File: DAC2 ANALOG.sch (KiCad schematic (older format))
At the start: 66 parts

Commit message: Add files via upload
Final - added testpoints, added MANF# data. Removed reconstruction filter
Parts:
- removed C? (x4): 6800pF, SciMod:EIA0603, symbol SciLib:C
- removed C? (x11): .1uF, SciMod:EIA0603, symbol Device:C
- removed C? (x2): 10uF, SciMod:EIA3528, symbol SciLib:CP1
- removed C?: 10pF, SciMod:EIA0603, symbol Device:C
- removed J?: SMB, SciMod:SMB 50, symbol SciLib:BNC
- removed J?: DAC BUFF, SciMod:SMB 50, symbol SciLib:BNC
- removed R? (x4): 10K, SciMod:EIA0603, symbol Device:R
- removed R? (x2): 33, SciMod:EIA0402, symbol SciLib:R
- removed TP?: VrefP, SciMod:TESTPOINT, symbol Connector:TestPoint
- removed TP?: VrefN, SciMod:TESTPOINT, symbol Connector:TestPoint
- removed TP?: AGND, SciMod:TESTPOINT, symbol Connector:TestPoint
- removed U?: OPA277, SOIC127P600X175-8N, symbol SciLib:OPA277
- added AGND, DAC: TST, TESTPOINT, symbol SciLib:TST
- added C? (x11): .1uF, SciMod:EIA0603, symbol Device:C
- added C? (x2): 10uF, SciMod:EIA3528, symbol SciLib:CP1
- added C? (x2): 6800pF, SciMod:EIA0805, symbol SciLib:C
- added R?: 0, SciMod:EIA0603, symbol SciLib:R
- added R? (x4): 10K, SciMod:EIA0603, symbol Device:R
- added R? (x2): 33, SciMod:EIA0402, symbol SciLib:R
- added TP?: AD IN, TESTPOINT, symbol SciLib:TST
- added TP?: VRP, TESTPOINT, symbol SciLib:TST
- added TP?: VRN, SciMod:TESTPOINT, symbol SciLib:TST
- C?: footprint SciMod:EIA0603 -> SciMod:EIA0805; Description CAP .1MF 10V 10% X7R EIA0603 -> 6800pF ±2% 50V Ceramic Capacitor C0G, NP0 0805; MANF# (none) -> GRM2195C1H682GA01D; Mfg AVX -> (none); Mfg Pn 0603YC104KAT2A -> (none); Partnum 10954 -> (none)
- C?: Description CAP .1MF 10V 10% X7R EIA0603 -> 47µF ±20% 6.3V Ceramic Capacitor X7R 1210; MANF# (none) -> C1210C476M9RACTU; Mfg AVX -> (none); Mfg Pn 0603YC104KAT2A -> (none); Partnum 10954 -> (none)
- C?: MANF# (none) -> 0603YC104KAT2A; Mfg Pn 0603YC104KAT2A -> (none)
- C?: MANF# (none) -> GRM188R71A105KA61D
- C?: Field4 (none) -> GRM188R71A105KA61D
- C? (x4): Description ?????? -> AVX Tant; MANF# (none) -> TAJB106K016RNJ; Partnum XXXXX -> (none)
- C?: Description ?????? -> AVX Tant; Partnum XXXXX -> TAJB106K016RNJ
- C?: Field5 (none) -> CAP CER 0.1UF 25V X8R 0603; MANF# (none) -> C1608X8R1E104K080AA
- H1, H2: renamed from H?; Description ?????? -> (none); Partnum XXXXX -> (none)
- J?: Description ?????? -> (none); MANF# (none) -> Scientech part; Partnum XXXXX -> (none)
- R? (x2): Description ?????? -> RES SMD 30.1 OHM 0.1% 1/6W 0603; MANF# (none) -> RP73PF1J30R1BTDF; Partnum XXXXX -> (none)
- R?: Field5 (none) -> RES SMD 10K OHM 1% 1/10W 0603; MANF# (none) -> ERJ-3EKF1002V
- R?: Field5 (none) -> RES SMD 5K OHM 0.1% 0.15W 0603 25ppm; MANF# (none) -> PNM0603E5001BST5
- R?: Description ?????? -> (none); MANF# (none) -> RC0402FR-0733RL; Partnum XXXXX -> (none)
- R? (x2): Description ?????? -> (none); Partnum XXXXX -> (none)
- R?: Field5 (none) -> RES 10K OHM 0.1% 1/8W 0805 25ppm; MANF# (none) -> ERA-6AEB103V
- Rs?: MANF# (none) -> Scientech
- U?: Field7 AD5791ARUZ-ND -> (none); MANF# (none) -> AD5791ARUZ-ND
- U?: footprint SciMod:SOIC127P-8 -> SciMod:ADA4077-2BRZ-R7; Description IC OPA2350 DUAL OP AMP HISPEED RRIO 8P SOIC -> IC OPAMP GP 2 CIRCUIT 8SOIC; MANF# (none) -> ADA4077-2BRZ-R7; Mfg TEXAS INSTRUMENTS -> Analog Devices; Mfg Pn OPA2350UA -> ADA4077-2BRZ-R7; Partnum XXXXX -> (none)
- U?: footprint SciMod:ADA4077-1BRZ -> SciMod:ADA4077-2BRZ-R7; Description IC OPA2350 DUAL OP AMP HISPEED RRIO 8P SOIC -> IC OPAMP GP 2 CIRCUIT 8SOIC; MANF# (none) -> ADA4077-2BRZ-R7; Mfg TEXAS INSTRUMENTS -> Analog Devices; Mfg Pn OPA2350UA -> (none); Partnum XXXXX -> (none)
- U?: MANF# (none) -> OPA277U; Mfg Pn OPA277U -> (none); Partnum 10986 -> (none)
- U?: MANF# (none) -> LT1010CT; Mfg Pn LT1010CT -> (none)
- U?: MANF# (none) -> LTC6655BHMS8-5#PBF
- U?: footprint SciMod:SOIC127P-8 -> SciMod:ADA4077-2BRZ-R7
- U?: footprint SciMod:ADA4077-1BRZ -> SciMod:ADA4077-2BRZ-R7; Description IC OPA2350 DUAL OP AMP HISPEED RRIO 8P SOIC -> (none); Mfg TEXAS INSTRUMENTS -> (none); Mfg Pn OPA2350UA -> (none); Partnum XXXXX -> (none)
- U?: MANF# (none) -> LTC6363IMS8#TRPBF
- U?: Description IC OPA277 OPAMP DUAL 8P SOIC -> (none); MANF# (none) -> AD8675ARZ; Mfg TEXAS INSTR -> (none); Mfg Pn OPA277U -> (none); Partnum 10986 -> (none)
- U?: footprint (none) -> SciMod:LTC2500CDKD-32-TRPBF; MANF# (none) -> LTC2500CDKD-32#PBF
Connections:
- wire segments 326 -> 324
- no-connect marks 14 -> 12
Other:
- note added: "+5VDC"
- note added: "-5VDC"
- note added: "References from LT6655 ckt below"
- note added: "Select the A/D input by installing only one of these."
- note added: "This is a bipolar +/- 5VDC signal."
- note added: "This is from the LTC2500-32 data sheet page 17."
- note added: "This reference block is right out of the AD5791EVAL circuit."
- note added: "This whole chunk is from the AD5791 evaluation module."

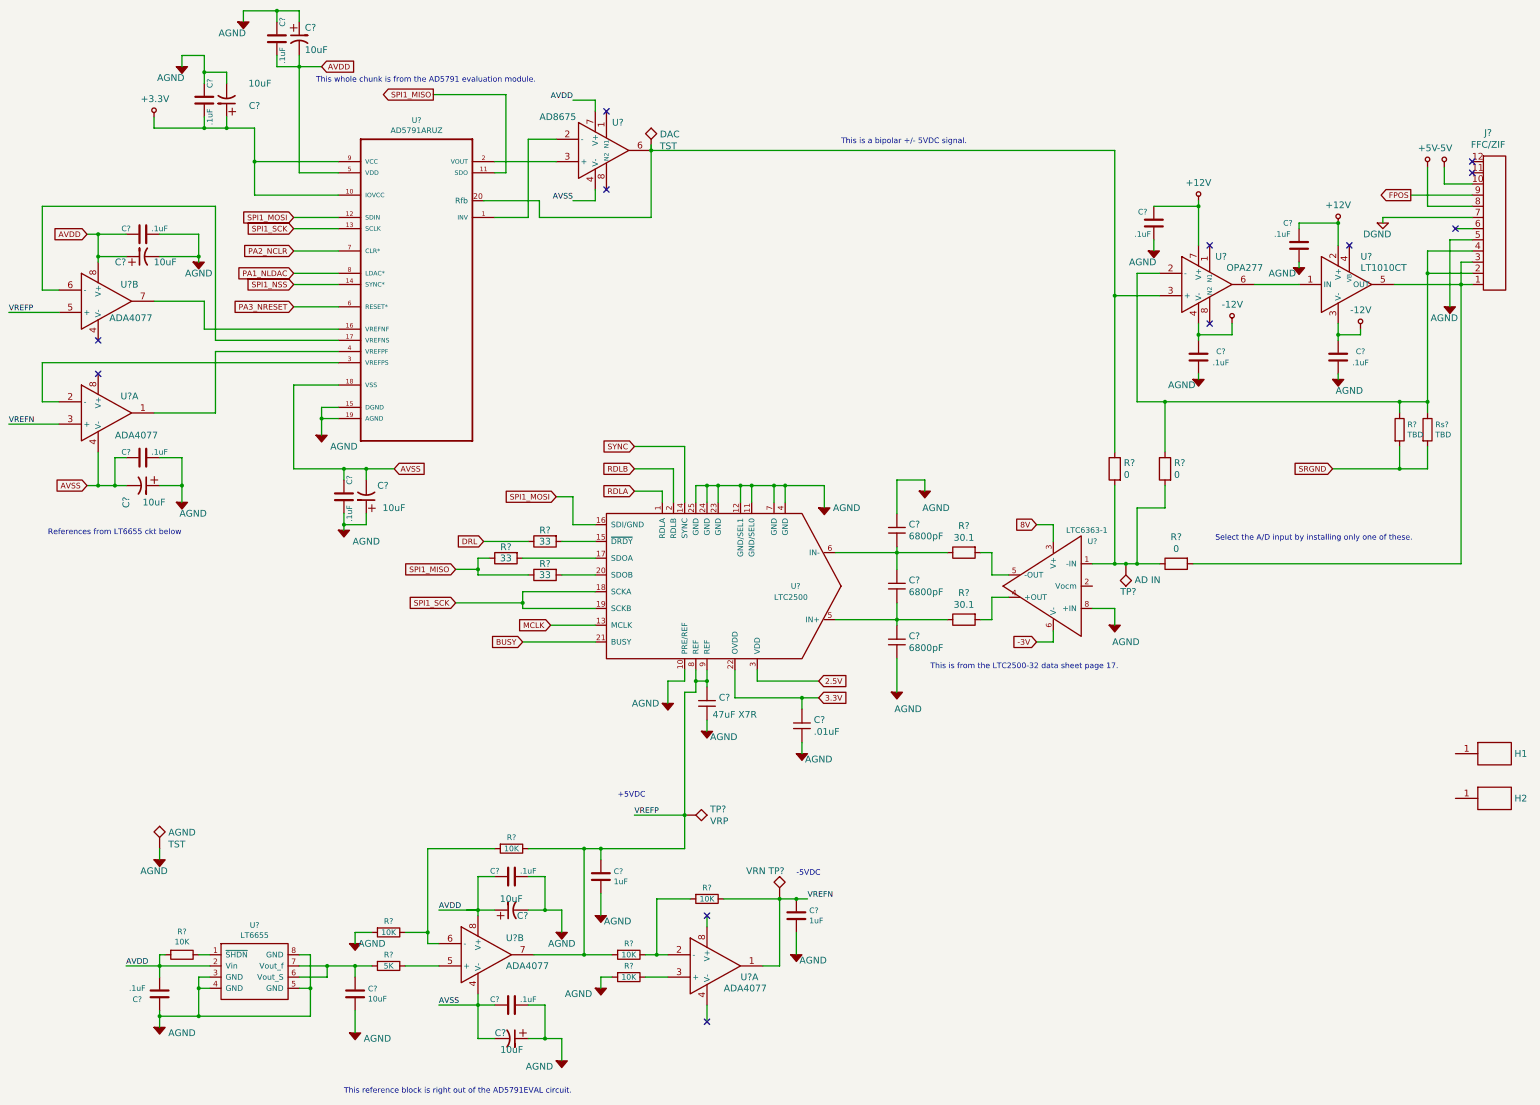
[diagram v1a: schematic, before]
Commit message: Added the analog portion to the board. Added as schematic sheet.
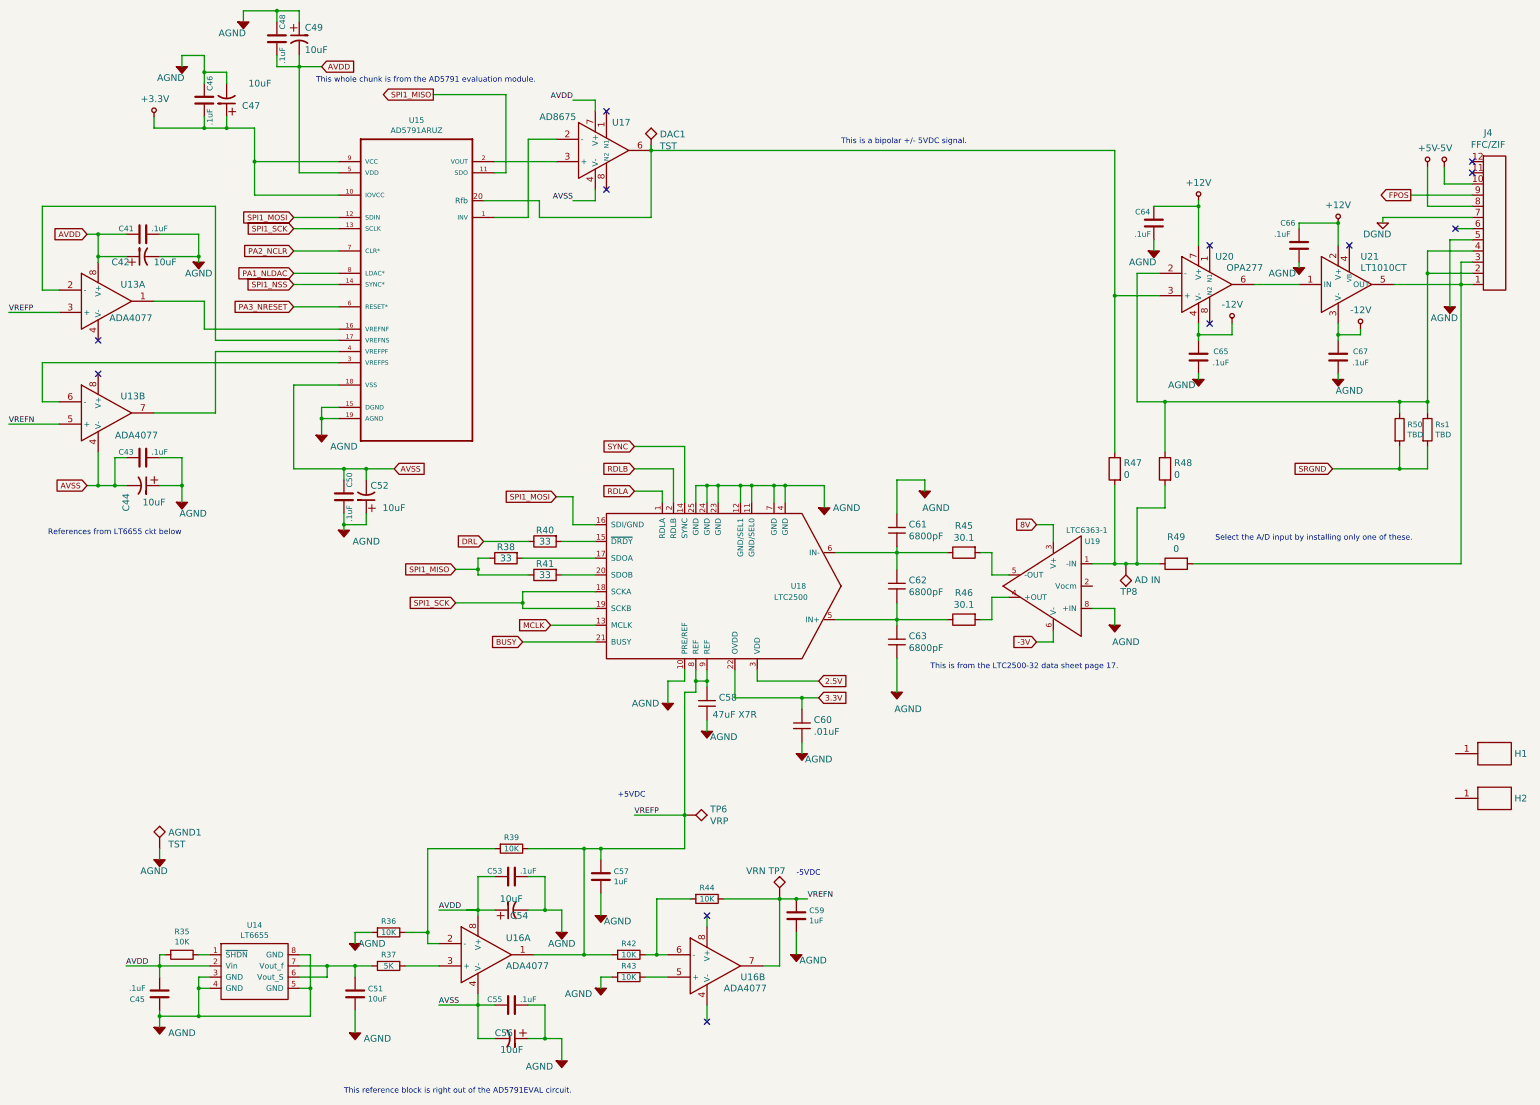
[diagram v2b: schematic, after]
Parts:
- AGND1: renamed from AGND; footprint TESTPOINT -> (none)
- DAC1: renamed from DAC; footprint TESTPOINT -> (none)
- TP6, TP8: renamed from TP?; footprint TESTPOINT -> (none)
- U21: renamed from U?; footprint TO220T-INV -> (none)
- gave numbers to parts that had none: 54
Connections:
- net VREFN: now also U13.5 (+), U16.7; no longer U13.3 (+), U16.1
- net VREFP: now also U13.3 (+), U16.1; no longer U13.5 (+), U16.7
- net at U15.16 (VREFNF): now also U13.1; no longer U13.7
- net at U15.17 (VREFNS): now also U13.2 (-); no longer U13.6 (-)
- net at U15.3 (VREFPS): now also U13.6 (-); no longer U13.2 (-)
- net at U15.4 (VREFPF): now also U13.7; no longer U13.1
- net at R37.1: now also U16.3 (+); no longer U16.5 (+)
- net at R36.1, R39.2: now also U16.2 (-); no longer U16.6 (-)
- net at R42.1, R44.2: now also U16.6 (-); no longer U16.2 (-)
- net at R43.1: now also U16.5 (+); no longer U16.3 (+)
